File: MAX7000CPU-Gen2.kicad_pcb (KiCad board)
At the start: 2 copper layers, 148.5 x 122 mm, 96 parts, among them J1 JTAG Conn_02x05_Odd_Even, J2 Instructions Conn_01x08_Male, J3 Module Input Conn_01x08_Male, J4 Module Output Conn_01x08_Male, J5 QPI Out Conn_01x08_Male, J6 QPI IN Conn_01x08_Male, J7 Conn_01x05_Male, J8 Barrel_Jack, SW1 Step SW_Push, SW2 CLK Mode SW_Push, SW3 Prog Select SW_DIP_x04, SW4 Reset SW_Push, U1 NE555P, U10 74LS573, U11 74LS241, U12 74LS241, U13 74LS573, U14 74LS573, U15 74LS573, U16 74LS573, U17 EPM7128slc84-15n, U18 LM2596S-5, U19 74LS241, U2 NE555P, U20 74LS241, U3 NE555P, U4 CLVC1GX04MDRLREP, U5 EPM7128slc84-15n, U6 74LS573, U7 SN74HC161N, U8 SN74HC161N, U9 IDT7132, Y1 Crystal

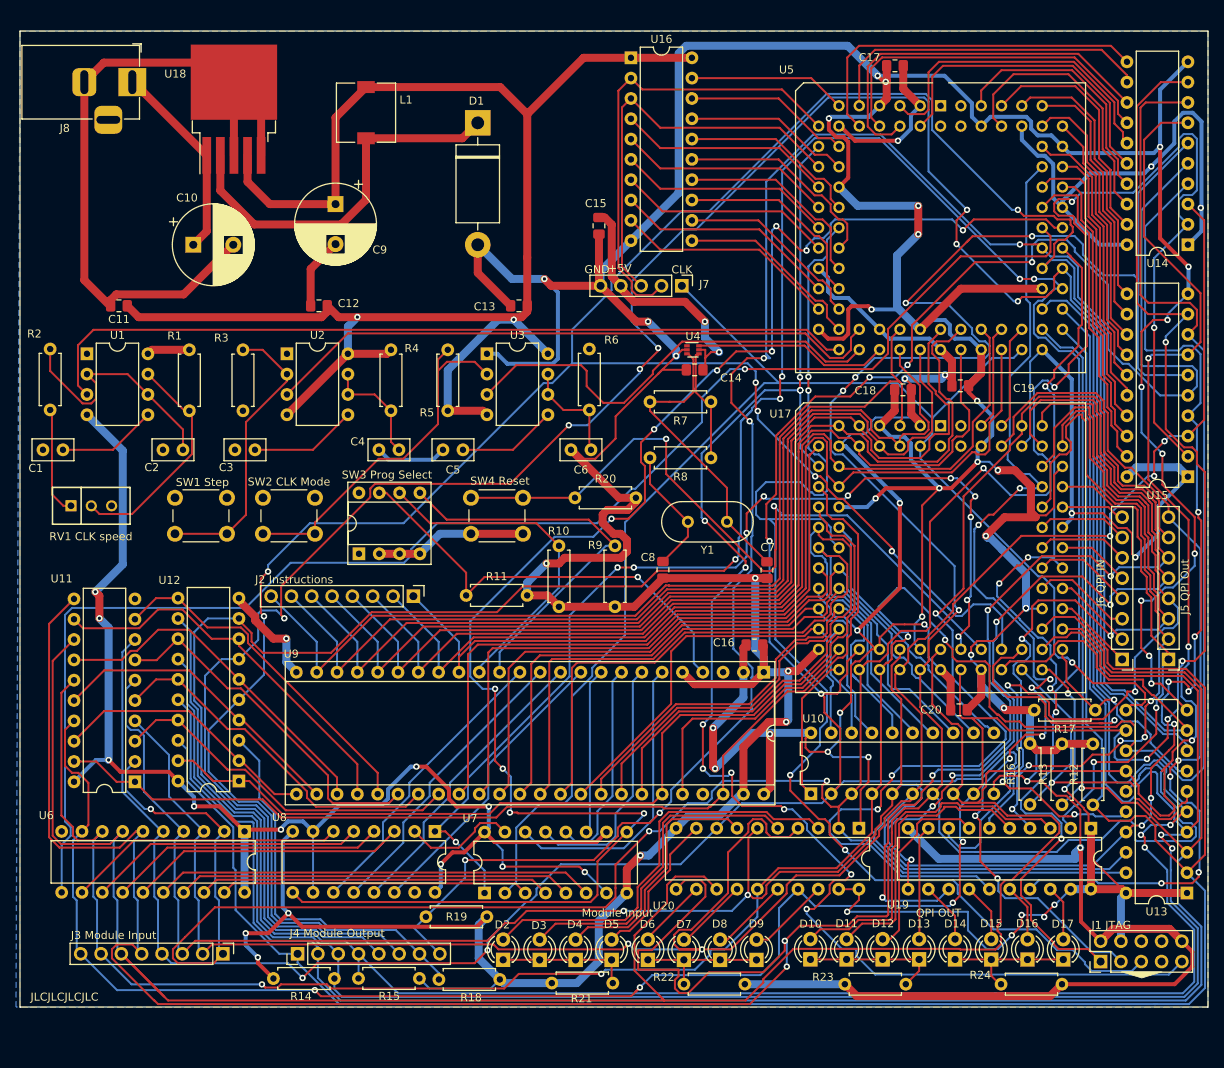
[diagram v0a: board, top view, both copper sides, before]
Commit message: Footprint Association
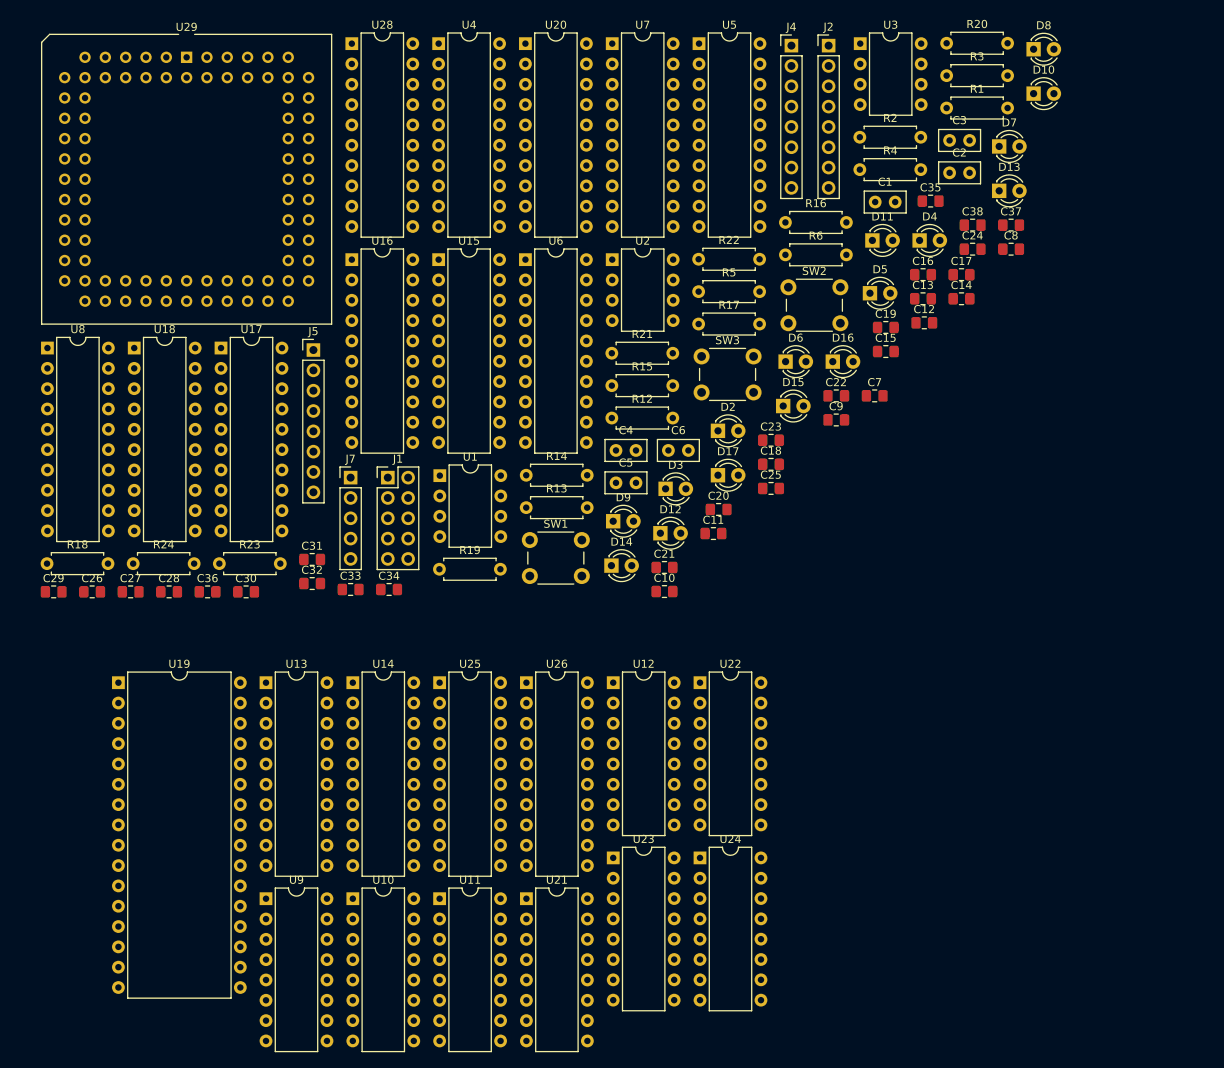
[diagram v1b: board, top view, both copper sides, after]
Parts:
- removed D1: 1N5822, Diode_THT:D_DO-201AD_P15.24mm_Horizontal
- removed J1 JTAG: Conn_02x05_Odd_Even, Connector_PinHeader_2.54mm:PinHeader_2x05_P2.54mm_Vertical
- removed J2 Instructions: Conn_01x08_Male, Connector_PinHeader_2.54mm:PinHeader_1x08_P2.54mm_Vertical
- removed J3 Module Input: Conn_01x08_Male, Connector_PinHeader_2.54mm:PinHeader_1x08_P2.54mm_Vertical
- removed J4 Module Output: Conn_01x08_Male, Connector_PinHeader_2.54mm:PinHeader_1x08_P2.54mm_Vertical
- removed J5 QPI Out: Conn_01x08_Male, Connector_PinHeader_2.54mm:PinHeader_1x08_P2.54mm_Vertical
- removed J6 QPI IN: Conn_01x08_Male, Connector_PinHeader_2.54mm:PinHeader_1x08_P2.54mm_Vertical
- removed J8: Barrel_Jack, Connector_BarrelJack:BarrelJack_Horizontal
- removed L1: 33u, Inductor_SMD:L_7.3x7.3_H3.5
- removed R10, R11, R9: 50K, Resistor_THT:R_Axial_DIN0207_L6.3mm_D2.5mm_P7.62mm_Horizontal
- removed R7: 2.2M, Resistor_THT:R_Axial_DIN0207_L6.3mm_D2.5mm_P7.62mm_Horizontal
- removed R8: 1K, Resistor_THT:R_Axial_DIN0207_L6.3mm_D2.5mm_P7.62mm_Horizontal
- removed RV1 CLK speed: 1M, MAX7000CPU:SIP460W50P254L970H980Q3P
- removed SW1 Step: SW_Push, Button_Switch_THT:SW_PUSH_6mm
- removed SW2 CLK Mode: SW_Push, Button_Switch_THT:SW_PUSH_6mm
- removed SW3 Prog Select: SW_DIP_x04, Package_DIP:DIP-8_W7.62mm_Socket
- removed SW4 Reset: SW_Push, Button_Switch_THT:SW_PUSH_6mm
- removed Y1: Crystal, Crystal:Crystal_HC49-4H_Vertical
- added C21: 100n, Capacitor_SMD:C_0805_2012Metric_Pad1.18x1.45mm_HandSolder, F.Cu at (97.6, 82.5)
- added C22: 100n, Capacitor_SMD:C_0805_2012Metric_Pad1.18x1.45mm_HandSolder, F.Cu at (119.0, 61.1)
- added C23: 100n, Capacitor_SMD:C_0805_2012Metric_Pad1.18x1.45mm_HandSolder, F.Cu at (110.9, 66.6)
- added C24: 100n, Capacitor_SMD:C_0805_2012Metric_Pad1.18x1.45mm_HandSolder, F.Cu at (136.1, 42.8)
- added C25: 100n, Capacitor_SMD:C_0805_2012Metric_Pad1.18x1.45mm_HandSolder, F.Cu at (110.9, 72.7)
- added C26: 100n, Capacitor_SMD:C_0805_2012Metric_Pad1.18x1.45mm_HandSolder, F.Cu at (26.0, 85.6)
- added C27: 100n, Capacitor_SMD:C_0805_2012Metric_Pad1.18x1.45mm_HandSolder, F.Cu at (30.8, 85.6)
- added C28: 100n, Capacitor_SMD:C_0805_2012Metric_Pad1.18x1.45mm_HandSolder, F.Cu at (35.6, 85.6)
- added C29: 100n, Capacitor_SMD:C_0805_2012Metric_Pad1.18x1.45mm_HandSolder, F.Cu at (21.2, 85.6)
- added C30: 100n, Capacitor_SMD:C_0805_2012Metric_Pad1.18x1.45mm_HandSolder, F.Cu at (45.3, 85.6)
- added C31: 100n, Capacitor_SMD:C_0805_2012Metric_Pad1.18x1.45mm_HandSolder, F.Cu at (53.5, 81.5)
- added C32: 100n, Capacitor_SMD:C_0805_2012Metric_Pad1.18x1.45mm_HandSolder, F.Cu at (53.5, 84.6)
- added C33: 100n, Capacitor_SMD:C_0805_2012Metric_Pad1.18x1.45mm_HandSolder, F.Cu at (58.3, 85.3)
- added C34: 100n, Capacitor_SMD:C_0805_2012Metric_Pad1.18x1.45mm_HandSolder, F.Cu at (63.1, 85.3)
- added C35: 100n, Capacitor_SMD:C_0805_2012Metric_Pad1.18x1.45mm_HandSolder, F.Cu at (130.8, 36.7)
- added C36: 100n, Capacitor_SMD:C_0805_2012Metric_Pad1.18x1.45mm_HandSolder, F.Cu at (40.4, 85.6)
- added C37: 100n, Capacitor_SMD:C_0805_2012Metric_Pad1.18x1.45mm_HandSolder, F.Cu at (140.9, 39.7)
- added C38: 100n, Capacitor_SMD:C_0805_2012Metric_Pad1.18x1.45mm_HandSolder, F.Cu at (136.1, 39.7)
- added J1: Conn_02x05_Odd_Even, Connector_PinHeader_2.54mm:PinHeader_2x05_P2.54mm_Vertical, F.Cu at (63.0, 71.3)
- added J2: Conn_01x08_Male, Connector_PinHeader_2.54mm:PinHeader_1x08_P2.54mm_Vertical, F.Cu at (118.1, 17.3)
- added J4: Conn_01x08_Male, Connector_PinHeader_2.54mm:PinHeader_1x08_P2.54mm_Vertical, F.Cu at (113.4, 17.3)
- added J5: Conn_01x08_Male, Connector_PinHeader_2.54mm:PinHeader_1x08_P2.54mm_Vertical, F.Cu at (53.7, 55.4)
- added SW1: SW_Push, Button_Switch_THT:SW_PUSH_6mm, F.Cu at (80.7, 79.1)
- added SW2: SW_Push, Button_Switch_THT:SW_PUSH_6mm, F.Cu at (113.0, 47.5)
- added SW3: SW_Push, Button_Switch_THT:SW_PUSH_6mm, F.Cu at (102.2, 56.2)
- added U21: CD4029BEE4, Package_DIP:DIP-16_W7.62mm, F.Cu at (80.3, 124.0)
- added U22: CD4029BEE4, Package_DIP:DIP-16_W7.62mm, F.Cu at (102.0, 97.0)
- added U23: CD4029BEE4, Package_DIP:DIP-16_W7.62mm, F.Cu at (91.2, 118.9)
- added U24: CD4029BEE4, Package_DIP:DIP-16_W7.62mm, F.Cu at (102.0, 118.9)
- added U25: 74LS241, Package_DIP:DIP-20_W7.62mm, F.Cu at (69.5, 97.0)
- added U26: 74LS241, Package_DIP:DIP-20_W7.62mm, F.Cu at (80.3, 97.0)
- added U28: 74LS574, Package_DIP:DIP-20_W7.62mm, F.Cu at (58.5, 17.1)
- added U29: EPM7128slc84-15n, Package_LCC:PLCC-84_THT-Socket, F.Cu at (37.8, 18.8)
- C10: value 680u -> 100n; footprint Capacitor_THT:CP_Radial_D10.0mm_P5.00mm -> Capacitor_SMD:C_0805_2012Metric_Pad1.18x1.45mm_HandSolder
- C7, C8: value 32p -> 100n
- C9: value 220u -> 100n; footprint Capacitor_THT:CP_Radial_D10.0mm_P5.00mm -> Capacitor_SMD:C_0805_2012Metric_Pad1.18x1.45mm_HandSolder
- U10: value 74LS573 -> CD4029BEE4; footprint Package_DIP:DIP-20_W7.62mm -> Package_DIP:DIP-16_W7.62mm
- U11, U12: value 74LS241 -> CD4029BEE4; footprint Package_DIP:DIP-20_W7.62mm -> Package_DIP:DIP-16_W7.62mm
- U13, U14, U15, U16: value 74LS573 -> 74LS241
- U17, U5: value EPM7128slc84-15n -> 74LS574; footprint Package_LCC:PLCC-84_THT-Socket -> Package_DIP:DIP-20_W7.62mm
- U18: value LM2596S-5 -> 74LS574; footprint Package_TO_SOT_SMD:TO-263-5_TabPin3 -> Package_DIP:DIP-20_W7.62mm
- U19: value 74LS241 -> AS6C1008-55PCN; footprint Package_DIP:DIP-20_W7.62mm -> Package_DIP:DIP-32_W15.24mm
- U20: value 74LS241 -> 74LS574
- U4: value CLVC1GX04MDRLREP -> 74LS574; footprint Package_TO_SOT_SMD:SOT-563 -> Package_DIP:DIP-20_W7.62mm
- U6: value 74LS573 -> 74LS574
- U7, U8: value SN74HC161N -> 74LS574; footprint Package_DIP:DIP-16_W7.62mm -> Package_DIP:DIP-20_W7.62mm
- U9: value IDT7132 -> CD4029BEE4; footprint Package_DIP:DIP-48_W15.24mm_Socket -> Package_DIP:DIP-16_W7.62mm
- moved U19 122.9 mm to (29.3, 97.0), turned to 0 degrees
- moved R24 120.5 mm to (31.1, 82.1)
- moved D8 120.4 mm to (143.7, 17.8), turned to 0 degrees
- moved U13 118.1 mm to (47.8, 97.0), turned to 0 degrees
- moved U14 117.9 mm to (58.6, 97.0), turned to 0 degrees
- moved D10 111.8 mm to (143.7, 23.3), turned to 0 degrees
- moved D7 109.1 mm to (139.4, 29.9), turned to 0 degrees
- moved U7 107.4 mm to (91.0, 17.1), turned to 0 degrees
- moved R2 106.8 mm to (122.0, 28.8), turned to 0 degrees
- moved U20 106.6 mm to (80.2, 17.1), turned to 0 degrees
- moved C1 106.1 mm to (123.9, 36.9), turned to 0 degrees
- moved C2 101.9 mm to (133.2, 33.2), turned to 0 degrees
- moved R23 100.6 mm to (41.9, 82.1), turned to 0 degrees
- moved D4 99.7 mm to (129.4, 41.7), turned to 0 degrees
- moved R1 99.4 mm to (132.8, 25.1), turned to 0 degrees
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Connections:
- C10 pad 1: Net-(C10-Pad1) -> +5V
- C7 pad 1: Net-(C7-Pad1) -> +5V
- C8 pad 1: Net-(C8-Pad1) -> +5V
- J7 pad 2: CarryOut -> SYNC
- J7 pad 3: A=B_Out -> STATE
- R12 pad 1: /O0 -> /B0
- R13 pad 1: /O1 -> /B1
- R14 pad 1: /O2 -> /B2
- R15 pad 1: /O3 -> /B3
- R16 pad 1: /O4 -> /B4
- R17 pad 1: /O5 -> /B5
- R18 pad 1: /O6 -> /B6
- R19 pad 1: /O7 -> /B7
- U10 pad 1: RamAddrEnable -> JumpEnable
- U10 pad 10: GND -> +5V
- U10 pad 11: RamAddrLoad -> Net-(U10-Pad11)
- U10 pad 12: /M7 -> Net-(U10-Pad12)
- U10 pad 13: /M5 -> Net-(U10-Pad13)
- U10 pad 14: /M4 -> Net-(U10-Pad14)
- U10 pad 15: /M1 -> Count
- U10 pad 16: /M2 -> +5V
- U10 pad 2: /I3 -> Net-(U10-Pad2)
- U10 pad 3: /I0 -> Net-(U10-Pad3)
- U10 pad 4: /I6 -> Net-(U10-Pad4)
- U10 pad 5: /I2 -> Net-(U10-Pad5)
- U10 pad 6: /I1 -> Net-(U10-Pad6)
- U10 pad 7: /I4 -> Net-(U10-Pad7)
- U10 pad 8: /I5 -> GND
- U10 pad 9: /I7 -> +5V
- U11 pad 1: MemWriteControl -> JumpEnable
- U11 pad 10: GND -> +5V
- U11 pad 11: /I4 -> Net-(U11-Pad11)
- U11 pad 13: /I5 -> Net-(U11-Pad13)
- U11 pad 15: /I6 -> Count
- U11 pad 16: Net-(U11-Pad16) -> +5V
- U11 pad 2: /I0 -> Net-(U11-Pad2)
- U11 pad 4: /I1 -> Net-(U11-Pad4)
- U11 pad 5: Net-(U11-Pad5) -> Net-(U10-Pad7)
- U11 pad 6: /I2 -> Net-(U11-Pad6)
- U11 pad 8: /I3 -> GND
- U11 pad 9: Net-(U11-Pad9) -> +5V
- U12 pad 1: MemOutControl -> JumpEnable
- U12 pad 10: GND -> +5V
- U12 pad 11: Net-(U11-Pad9) -> Net-(U12-Pad11)
- U12 pad 12: /O3 -> Net-(U12-Pad12)
- U12 pad 13: Net-(U11-Pad7) -> Net-(U12-Pad13)
- U12 pad 14: /O2 -> Net-(U12-Pad14)
- U12 pad 15: Net-(U11-Pad5) -> Count
- U12 pad 16: /O1 -> +5V
- U12 pad 2: Net-(U11-Pad18) -> Net-(U12-Pad2)
- U12 pad 3: /O7 -> Net-(U12-Pad3)
- U12 pad 4: Net-(U11-Pad16) -> Net-(U12-Pad4)
- U12 pad 5: /O6 -> Net-(U11-Pad7)
- U12 pad 6: Net-(U11-Pad14) -> Net-(U12-Pad6)
- U12 pad 7: /O5 -> Net-(U12-Pad7)
- U12 pad 8: Net-(U11-Pad12) -> GND
- U12 pad 9: /O4 -> +5V
- U13 pad 1: +5V -> CounterOutControl
- U13 pad 11: CLK -> Net-(U10-Pad6)
- U13 pad 12: /I7 -> /RA_L3
- U13 pad 13: /I6 -> Net-(U10-Pad11)
- U13 pad 14: /I5 -> /RA_L2
- U13 pad 15: /I4 -> Net-(U10-Pad14)
- U13 pad 16: /I3 -> /RA_L1
- U13 pad 17: /I2 -> Net-(U10-Pad2)
- U13 pad 18: /I1 -> /RA_L0
- U13 pad 19: /I0 -> CounterOutControl
- U13 pad 2: /O0 -> Net-(U13-Pad2)
- U13 pad 3: /O1 -> /RA_L7
- U13 pad 4: /O2 -> Net-(U13-Pad4)
- U13 pad 5: /O3 -> /RA_L6
- U13 pad 6: /O4 -> Net-(U13-Pad6)
- U13 pad 7: /O5 -> /RA_L5
- U13 pad 8: /O6 -> Net-(U13-Pad8)
- U13 pad 9: /O7 -> /RA_L4
- U14 pad 1: +5V -> CounterOutControl
- U14 pad 11: RegAControl -> Net-(U12-Pad6)
- U14 pad 12: /A7 -> /RA_H3
- U14 pad 13: /A6 -> Net-(U12-Pad11)
- U14 pad 14: /A5 -> /RA_H2
- U14 pad 15: /A4 -> Net-(U12-Pad14)
- U14 pad 16: /A3 -> /RA_H1
- U14 pad 17: /A2 -> Net-(U12-Pad2)
- U14 pad 18: /A1 -> /RA_H0
- U14 pad 19: /A0 -> CounterOutControl
- U14 pad 2: /I0 -> Net-(U11-Pad6)
- U14 pad 3: /I1 -> /RA_H7
- U14 pad 4: /I2 -> Net-(U11-Pad11)
- U14 pad 5: /I3 -> /RA_H6
- U14 pad 6: /I4 -> Net-(U11-Pad14)
- U14 pad 7: /I5 -> /RA_H5
- U14 pad 8: /I6 -> Net-(U11-Pad2)
- U14 pad 9: /I7 -> /RA_H4
- U15 pad 1: +5V -> GND
- U15 pad 11: RegBControl -> /B4
- U15 pad 12: /B7 -> /Im3
- U15 pad 13: /B6 -> /B5
- U15 pad 14: /B5 -> /Im2
- U15 pad 15: /B4 -> /B6
- U15 pad 16: /B3 -> /Im1
- U15 pad 17: /B2 -> /B7
- U15 pad 18: /B1 -> /Im0
- U15 pad 19: /B0 -> GND
- U15 pad 2: /I0 -> /B0
- U15 pad 3: /I1 -> /Im7
- U15 pad 4: /I2 -> /B1
- U15 pad 5: /I3 -> /Im6
- U15 pad 6: /I4 -> /B2
- U15 pad 7: /I5 -> /Im5
- U15 pad 8: /I6 -> /B3
- U15 pad 9: /I7 -> /Im4
- U16 pad 1: +5V -> GND
- U16 pad 11: FlagCLK -> /Qo4
- U16 pad 12: Flag5In -> /Iq3
- U16 pad 13: Flag4In -> /Qo5
- U16 pad 14: Flag3In -> /Iq2
- U16 pad 15: Flag2In -> /Qo6
- U16 pad 16: Flag1In -> /Iq1
- U16 pad 17: Flag0In -> /Qo7
- U16 pad 18: A=B_FlagIn -> /Iq0
- U16 pad 19: CarryFlagIn -> GND
- U16 pad 2: CarryOut -> /Qo0
- U16 pad 3: A=B_Out -> /Iq7
- U16 pad 4: Flag0Out -> /Qo1
- U16 pad 5: Flag1Out -> /Iq6
- U16 pad 6: Flag2Out -> /Qo2
- U16 pad 7: Flag3Out -> /Iq5
- U16 pad 8: Flag4Out -> /Qo3
- U16 pad 9: Flag5Out -> /Iq4
- U17 pad 1: Net-(U17-Pad1) -> RAM_Addr_Enable
- U17 pad 10: /Ins2 -> GND
- U17 pad 11: /Ins3 -> RAM_LowControl
- U17 pad 12: /M9 -> /RA_L7
- U17 pad 13: +5V -> /RA_L6
- U17 pad 14: TDI -> /RA_L5
- U17 pad 15: /Ins1 -> /RA_L4
- U17 pad 16: MemWriteControl -> /RA_L3
- U17 pad 17: /Ins0 -> /RA_L2
- U17 pad 18: MemOutControl -> /RA_L1
- U17 pad 19: GND -> /RA_L0
- U17 pad 2: Net-(U17-Pad2) -> /B0
- U17 pad 20: /M1 -> +5V
- U17 pad 3: +5V -> /B1
- U17 pad 4: CLK -> /B2
- U17 pad 5: /Ins7 -> /B3
- U17 pad 6: /Ins6 -> /B4
- U17 pad 7: GND -> /B5
- U17 pad 8: /Ins5 -> /B6
- U17 pad 9: /Ins4 -> /B7
- U18 pad 1: Net-(C10-Pad1) -> RAM_Addr_Enable
- U18 pad 2: Net-(D1-Pad1) -> /B0
- U18 pad 3: GND -> /B1
- U18 pad 4: +5V -> /B2
- U18 pad 5: GND -> /B3
- U19 pad 1: +5V -> Net-(U19-Pad1)
- U19 pad 10: GND -> /RA_L2
- U19 pad 11: /Qo4 -> /RA_L1
- U19 pad 12: /Iq3 -> /RA_L0
- U19 pad 13: /Qo5 -> /B0
- U19 pad 14: /Iq2 -> /B1
- U19 pad 15: /Qo6 -> /B2
- U19 pad 16: /Iq1 -> GND
- U19 pad 17: /Qo7 -> /B3
- U19 pad 18: /Iq0 -> /B4
- U19 pad 19: +5V -> /B5
- U19 pad 2: /Qo0 -> GND
- U19 pad 20: +5V -> /B6
- U19 pad 3: /Iq7 -> /RA_H6
- U19 pad 4: /Qo1 -> /RA_H4
- U19 pad 5: /Iq6 -> /RA_L7
- U19 pad 6: /Qo2 -> /RA_L6
- U19 pad 7: /Iq5 -> /RA_L5
- U19 pad 8: /Qo3 -> /RA_L4
- U19 pad 9: /Iq4 -> /RA_L3
- U20 pad 1: +5V -> GND
- U20 pad 11: /I4 -> InsRegControl
- U20 pad 12: /Im3 -> /Ins7
- U20 pad 13: /I5 -> /Ins6
- U20 pad 14: /Im2 -> /Ins5
- U20 pad 15: /I6 -> /Ins4
- U20 pad 16: /Im1 -> /Ins3
- U20 pad 17: /I7 -> /Ins2
- U20 pad 18: /Im0 -> /Ins1
- U20 pad 19: +5V -> /Ins0
- U20 pad 2: /I0 -> /B0
- U20 pad 3: /Im7 -> /B1
- U20 pad 4: /I1 -> /B2
- U20 pad 5: /Im6 -> /B3
- U20 pad 6: /I2 -> /B4
- U20 pad 7: /Im5 -> /B5
- U20 pad 8: /I3 -> /B6
- U20 pad 9: /Im4 -> /B7
- U4 pad 1: Net-(U4-Pad1) -> MainRegOutputControl
- U4 pad 2: GND -> /B0
- U4 pad 3: Net-(C7-Pad1) -> /B1
- U4 pad 4: Net-(R7-Pad1) -> /B2
- U4 pad 5: +5V -> /B3
- U4 pad 6: FastCLK -> /B4
- U5 pad 1: Net-(U5-Pad1) -> GND
- U5 pad 10: RegAControl -> GND
- U5 pad 11: CarryFlagIn -> RegAControl
- U5 pad 12: CarryOut -> /rA7
- U5 pad 13: +5V -> /rA6
- U5 pad 14: TDI -> /rA5
- U5 pad 15: A=B_FlagIn -> /rA4
- U5 pad 16: A=B_Out -> /rA3
- U5 pad 17: Flag0In -> /rA2
- U5 pad 18: Flag0Out -> /rA1
- U5 pad 19: GND -> /rA0
- U5 pad 2: Net-(U5-Pad2) -> /B0
- U5 pad 20: Flag1Out -> +5V
- U5 pad 3: +5V -> /B1
- U5 pad 4: /A3 -> /B2
- U5 pad 5: /A4 -> /B3
- U5 pad 6: /A6 -> /B4
- U5 pad 7: GND -> /B5
- U5 pad 8: /A5 -> /B6
- U5 pad 9: /A7 -> /B7
- U6 pad 1: +5V -> GND
- U6 pad 11: JumpRegLoad -> RegBControl
- U6 pad 12: Net-(U6-Pad12) -> /rB7
- U6 pad 13: Net-(U6-Pad13) -> /rB6
- U6 pad 14: Net-(U6-Pad14) -> /rB5
- U6 pad 15: Net-(U6-Pad15) -> /rB4
- U6 pad 16: Net-(U6-Pad16) -> /rB3
- U6 pad 17: Net-(U6-Pad17) -> /rB2
- U6 pad 18: Net-(U6-Pad18) -> /rB1
- U6 pad 19: Net-(U6-Pad19) -> /rB0
- U6 pad 2: /I0 -> /B0
- U6 pad 3: /I1 -> /B1
- U6 pad 4: /I2 -> /B2
- U6 pad 5: /I3 -> /B3
- U6 pad 6: /I4 -> /B4
- U6 pad 7: /I5 -> /B5
- U6 pad 8: /I6 -> /B6
- U6 pad 9: /I7 -> /B7
- U7 pad 1: CounterReset -> GND
- U7 pad 10: +5V -> GND
- U7 pad 11: /C3 -> LOWJumpRegLoad
- U7 pad 12: /C2 -> Net-(U10-Pad3)
- U7 pad 13: /C1 -> Net-(U10-Pad13)
- U7 pad 14: /C0 -> Net-(U10-Pad12)
- U7 pad 15: Net-(U7-Pad15) -> Net-(U10-Pad4)
- U7 pad 16: +5V -> Net-(U7-Pad16)
- U7 pad 2: CLK -> /B0
- U7 pad 3: Net-(U6-Pad19) -> /B1
- U7 pad 4: Net-(U6-Pad18) -> /B2
- U7 pad 5: Net-(U6-Pad17) -> /B3
- U7 pad 6: Net-(U6-Pad16) -> /B4
- U7 pad 7: +5V -> /B5
- U7 pad 8: GND -> /B6
- U7 pad 9: JumpEnable -> /B7
- U8 pad 1: CounterReset -> GND
- U8 pad 10: +5V -> GND
- U8 pad 11: /C7 -> HIGHJumpRegLoad
- U8 pad 12: /C6 -> Net-(U12-Pad3)
- U8 pad 13: /C5 -> Net-(U12-Pad13)
- U8 pad 14: /C4 -> Net-(U12-Pad12)
- U8 pad 15: Net-(U8-Pad15) -> Net-(U12-Pad4)
- U8 pad 16: +5V -> Net-(U11-Pad3)
- U8 pad 2: Net-(U7-Pad15) -> /B0
- U8 pad 3: Net-(U6-Pad15) -> /B1
- U8 pad 4: Net-(U6-Pad14) -> /B2
- U8 pad 5: Net-(U6-Pad13) -> /B3
- U8 pad 6: Net-(U6-Pad12) -> /B4
- U8 pad 7: +5V -> /B5
- U8 pad 8: GND -> /B6
- U8 pad 9: JumpEnable -> /B7
- U9 pad 1: GND -> JumpEnable
- U9 pad 10: /C4 -> +5V
- U9 pad 11: /C5 -> Net-(U13-Pad4)
- U9 pad 12: /C6 -> Net-(U7-Pad18)
- U9 pad 13: /C7 -> Net-(U7-Pad17)
- U9 pad 14: /P1 -> Net-(U13-Pad6)
- U9 pad 15: /P2 -> Count
- U9 pad 16: /Ins0 -> +5V
- U9 pad 2: +5V -> Net-(U13-Pad8)
- U9 pad 3: Net-(U9-Pad3) -> Net-(U7-Pad16)
- U9 pad 4: /P3 -> Net-(U7-Pad19)
- U9 pad 6: /C0 -> Net-(U13-Pad2)
- U9 pad 7: /C1 -> Net-(U10-Pad5)
- U9 pad 8: /C2 -> GND
- U9 pad 9: /C3 -> +5V
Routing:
- net GND: track 1051.5 -> 0.00 mm, vias 40 -> 0
- net +5V: track 883.0 -> 0.00 mm, vias 37 -> 0
- net /I4: track 464.4 -> 0.00 mm, vias 7 -> 0
- net /I5: track 394.1 -> 0.00 mm, vias 3 -> 0
- net /O6: track 370.5 -> 0.00 mm, vias 7 -> 0
- net /I3: track 361.6 -> 0.00 mm, vias 9 -> 0
- net /I0: track 357.0 -> 0.00 mm, vias 7 -> 0
- net /I6: track 339.7 -> 0.00 mm, vias 4 -> 0
- net /O4: track 334.5 -> 0.00 mm, vias 6 -> 0
- net /O7: track 322.3 -> 0.00 mm, vias 5 -> 0
- net /I7: track 318.2 -> 0.00 mm, vias 8 -> 0
- net /I2: track 315.6 -> 0.00 mm, vias 9 -> 0
- net /O5: track 313.3 -> 0.00 mm, vias 8 -> 0
- net /I1: track 311.6 -> 0.00 mm, vias 5 -> 0
- net /O2: track 310.4 -> 0.00 mm, vias 2 -> 0
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- removed copper zone on F.Cu, net +5V
- removed copper zone on B.Cu, net GND
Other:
- board outline removed
- board text removed: "+5V"
- board text removed: "CLK"
- board text removed: "GND"
- board text removed: "JLCJLCJLCJLC"
- board text removed: "Module Input"
- board text removed: "QPI OUT"
